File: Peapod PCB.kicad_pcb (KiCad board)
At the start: 2 copper layers, 70.9 x 27.2 mm, 20 parts, among them U1 ESP8266

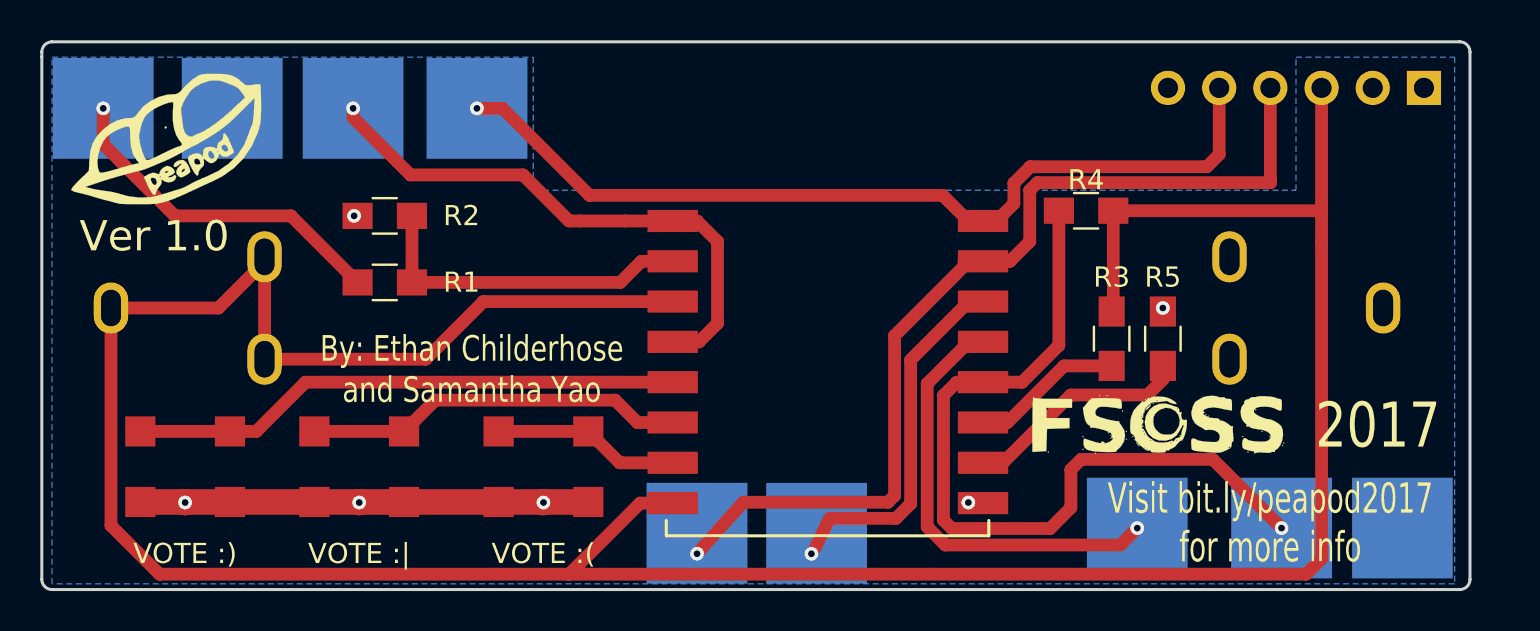
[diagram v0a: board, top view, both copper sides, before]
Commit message: Updated logo, year, names
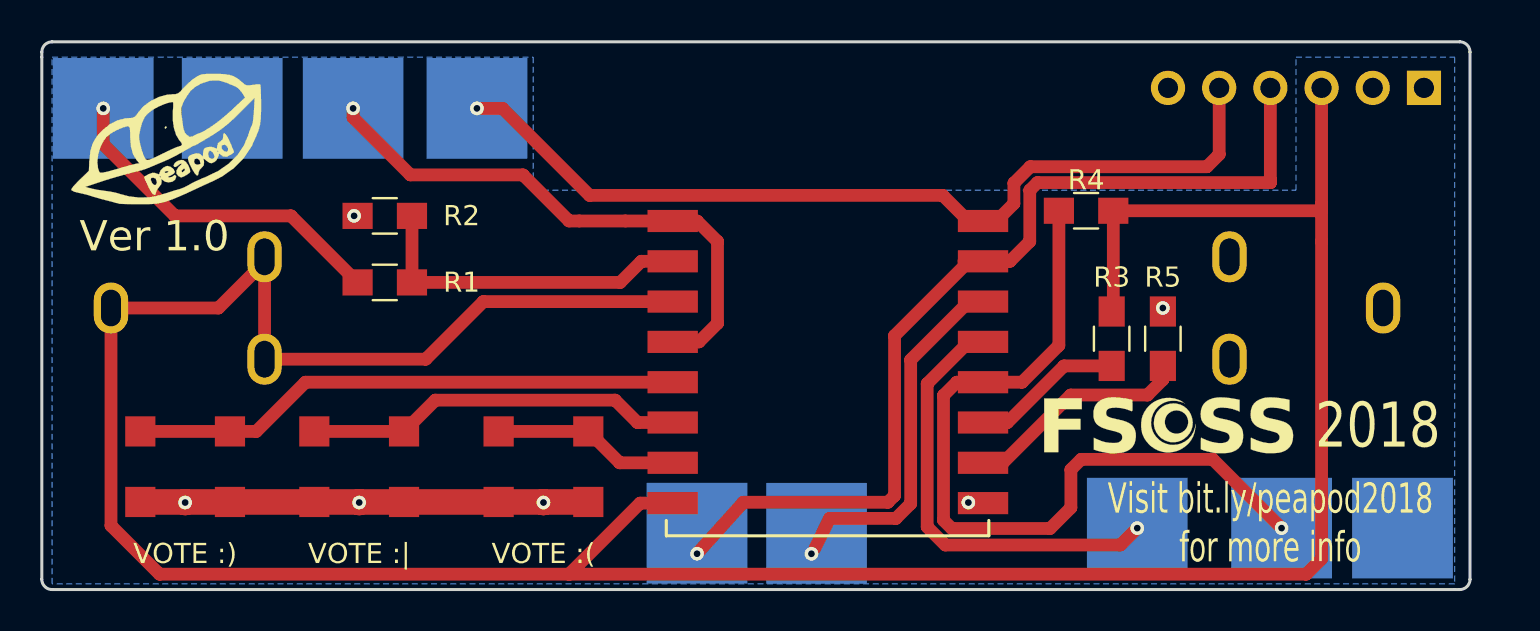
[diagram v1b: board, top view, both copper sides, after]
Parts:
- FTDI 3.3V Vcc ONLY!: renamed from FTDI 3.3V
- G***: footprint mod:fsoss -> logo:fsoss_logo4
- moved G*** 0.38 mm to (208.8, 45.1)
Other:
- board text added: "2018"
- board text added: "Hardware and firmware by Ethan Childerhose, Samantha Yao, Eric Brauer, and Chris Tyler"
- board text added: "Visit bit.ly/peapod2018 for more info"
- board text removed: "2017"
- board text removed: "By: Ethan Childerhose and Samantha Yao"
- board text removed: "Visit bit.ly/peapod2017 for more info"
